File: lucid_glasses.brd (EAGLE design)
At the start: 21.3 x 15.9 mm, 7 parts, among them IC1 AT90LS2343P, IC2 786TV

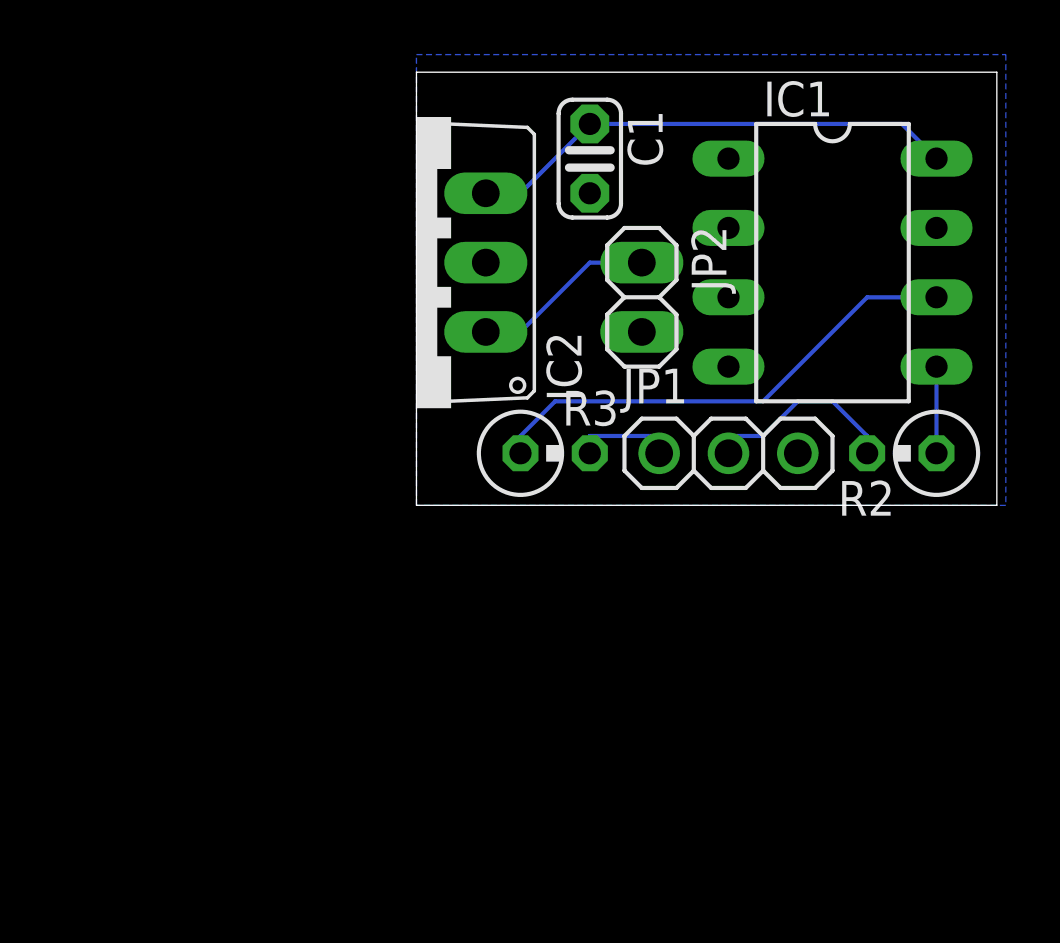
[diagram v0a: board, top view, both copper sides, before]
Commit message: Updated board for smt with coin cell battery.
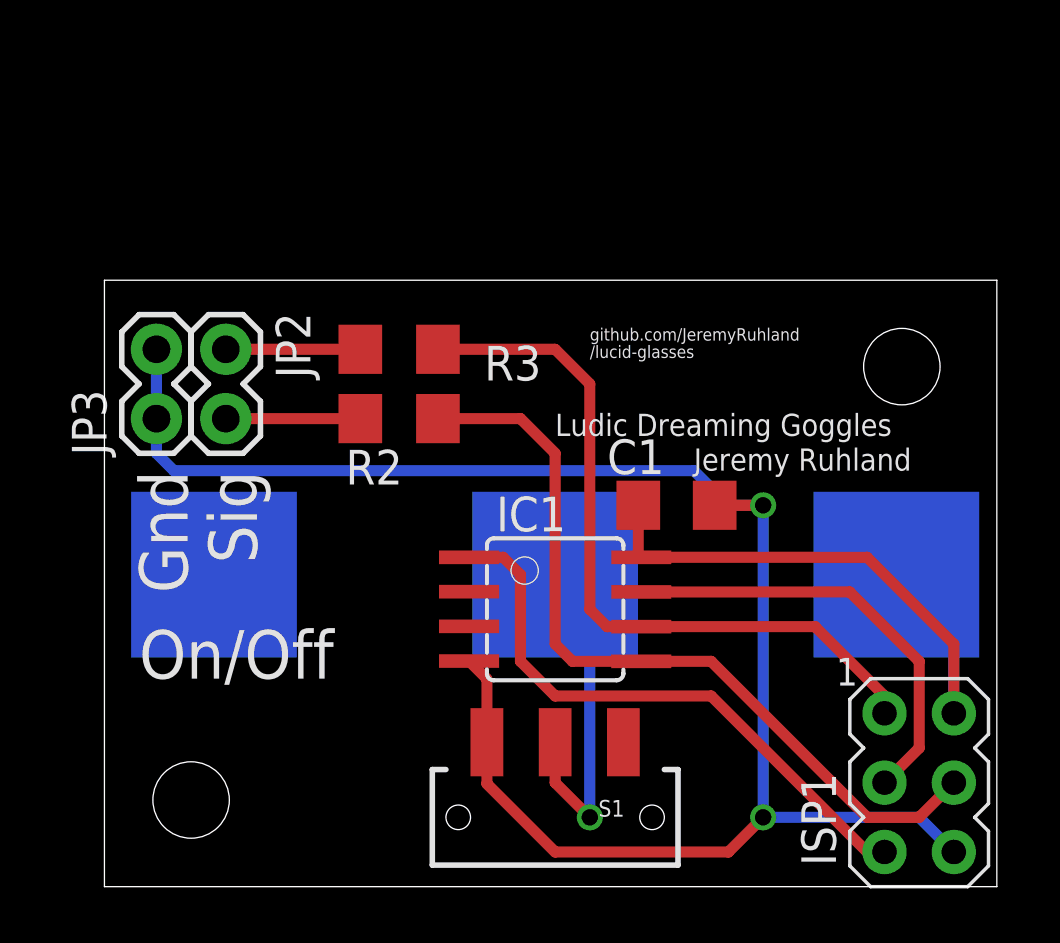
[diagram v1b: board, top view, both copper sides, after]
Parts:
- removed IC2: 786TV, linear:TO220V
- removed JP1: (no value), adafruit:1X03
- added BAT1: (no value), sparkfun:BATTCON_20MM
- added ISP1: AVRISP-6, adafruit:AVRISP
- added JP3: (no value), sparkfun:1X02
- added S1: (no value), sparkfun:SWITCH-SPDT-SMD
- C1: device adafruit:C025-024X044 -> adafruit:C1206
- IC1: value AT90LS2343P -> AT90LS2343S; device atmel:DIL08 -> atmel:SOIC8
- JP2: device pinhead:1X02 -> sparkfun:1X02
- R2, R3: device resistor:0309V -> resistor:R1206
- moved R2 18.5 mm to (-0.64, 6.99)
- moved IC1 16.3 mm to (5.08, 0.00)
- moved JP2 15.4 mm to (-6.99, 9.53)
- moved C1 13.1 mm to (9.53, 3.81), turned to 0 degrees
- moved R3 6.87 mm to (-0.64, 9.53), turned to 180 degrees
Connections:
- removed net +12V: IC2.1, JP2.1
- removed net N$3: IC1.6, R3.1
- new net MISO: IC1.6, ISP1.1, R3.1
- new net MOSI: IC1.5, ISP1.4, R2.1
- new net RST: IC1.1, ISP1.5
- new net SCK: IC1.7, ISP1.3
- net GND: now also ISP1.6, JP3.1, JP3.2, S1.3; no longer IC2.2, JP1.3, JP2.2
- net N$1: now also JP2.1; no longer JP1.1
- net N$2: now also BAT1.2, S1.2; no longer IC1.5, R2.1
- net N$4: now also JP2.2; no longer JP1.2
- net VCC: now also BAT1.1, ISP1.2; no longer IC2.3
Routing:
- net GND: track 0.00 -> 64.0 mm, vias 0 -> 2
- net MOSI: track 0.00 -> 29.6 mm
- net MISO: track 0.00 -> 27.1 mm
- net RST: track 0.00 -> 21.6 mm
- net N$3: track 18.0 -> 0.00 mm
- net SCK: track 0.00 -> 16.2 mm
- net N$2: track 3.18 -> 12.7 mm, vias 0 -> 1
- net +12V: track 6.77 -> 0.00 mm
- net VCC: track 18.1 -> 23.2 mm
- net N$4: track 7.40 -> 4.93 mm
- net N$1: track 3.81 -> 4.93 mm
- removed copper zone on layer 16, net GND
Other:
- board size 21.3 x 15.9 mm -> 32.7 x 22.2 mm
- board text added: "/lucid-glasses"
- board text added: "Gnd"
- board text added: "Jeremy Ruhland"
- board text added: "Ludic Dreaming Goggles"
- board text added: "On/Off"
- board text added: "Sig"
- board text added: "github.com/JeremyRuhland"
